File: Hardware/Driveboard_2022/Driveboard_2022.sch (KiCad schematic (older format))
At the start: 107 parts, among them SW1 SW_Push, SW2 SW_Push, SW3 SW_Push, SW4 SW_SPST, SW5 SW_Push, SW6 SW_Push, SW7 SW_Push, U1 TM4C129E_Launchpad, U2 MAX_3232, U3 MAX_3232, U4 MAX_3232, U5 OKI 3V3, U6 OKI 5V

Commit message: Removed Encoder, Fixed Resistor Values
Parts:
- removed Conn1, Conn2, Conn3, Conn4, Conn5, Conn6: Molex_uF_S_03, MRDT_Connectors:MOLEX_uF_S_03_Horizontal, symbol MRDT_Connectors:Molex_uF_S_03
- removed LED29, LED30, LED31, LED32, LED33, LED34: Blue, symbol Device:LED
- removed R29, R30, R31, R32, R33, R34: 330, symbol Device:R
- Conn13: symbol MRDT_Connectors:AndersonPP -> Driveboard_2022-rescue:AndersonPP-MRDT_Connectors
- R10: value 1k -> 330
- R11, R12, R13, R14, R15, R16, R8: value 330 -> 43
- R17, R18, R19, R20, R21, R22, R23, R24, R25, R26, R27, R28, R9: value 500 -> 100
- U2, U3, U4: symbol MRDT_ICs:MAX_3232 -> Driveboard_2022-rescue:MAX_3232-MRDT_ICs
- U5, U6: symbol MRDT_Devices:OKI -> Driveboard_2022-rescue:OKI-MRDT_Devices
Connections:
- net labels removed: BL_PWM, BR_PWM, FL_PWM, FR_PWM, ML_PWM, MR_PWM
- wire segments 373 -> 313
- no-connect marks 43 -> 49
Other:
- moved on the sheet: Conn10, Conn11, Conn12, Conn7, Conn8, Conn9

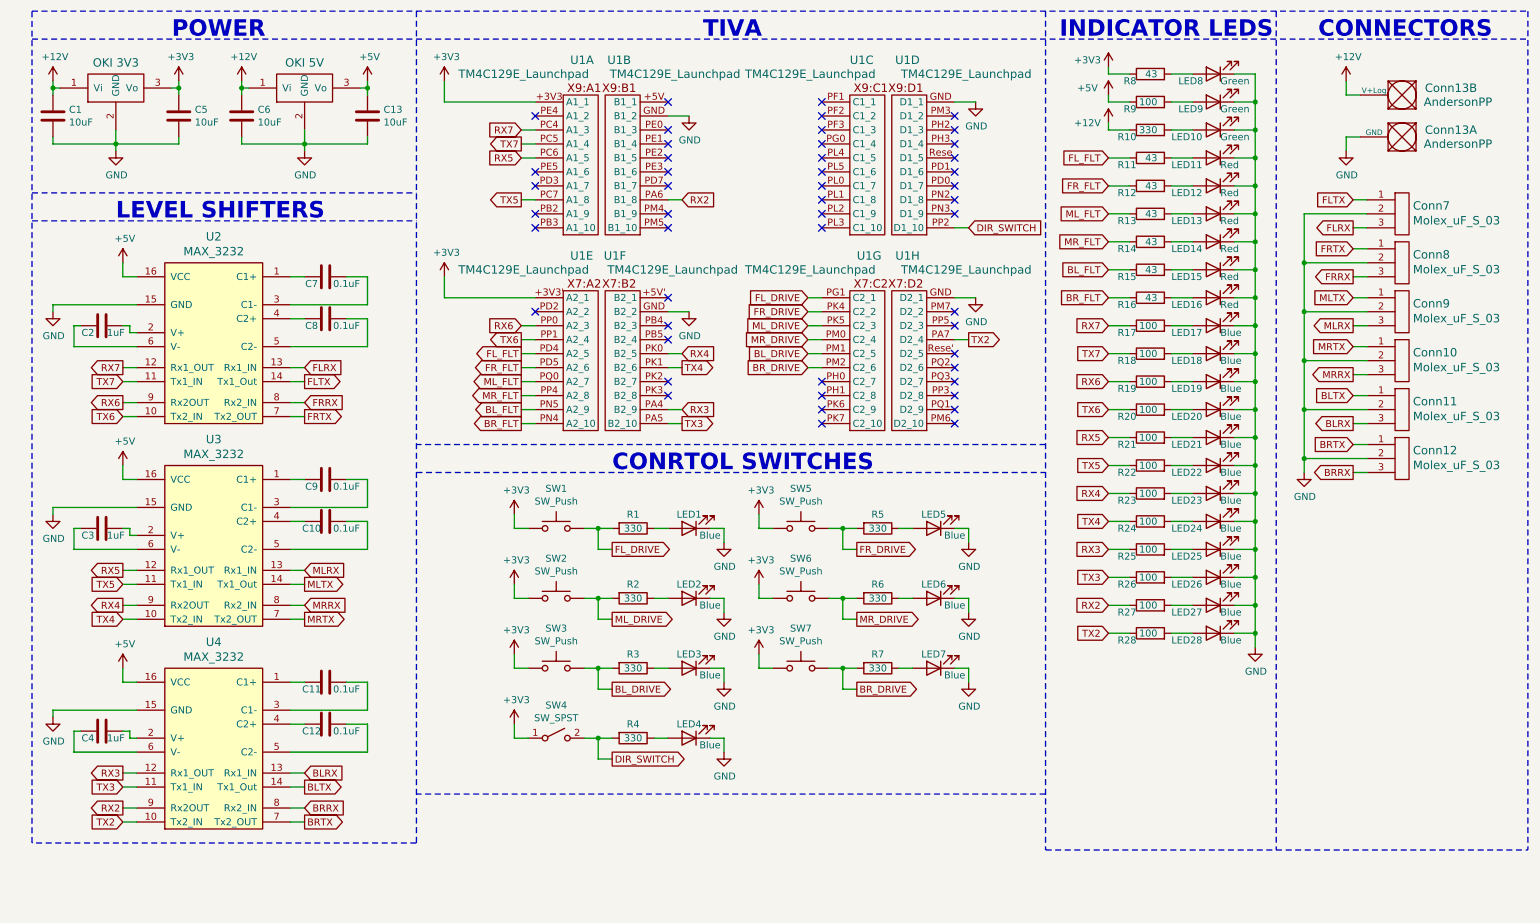
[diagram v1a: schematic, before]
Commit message: Added VESC Connectors, Fixed Switch Resistors
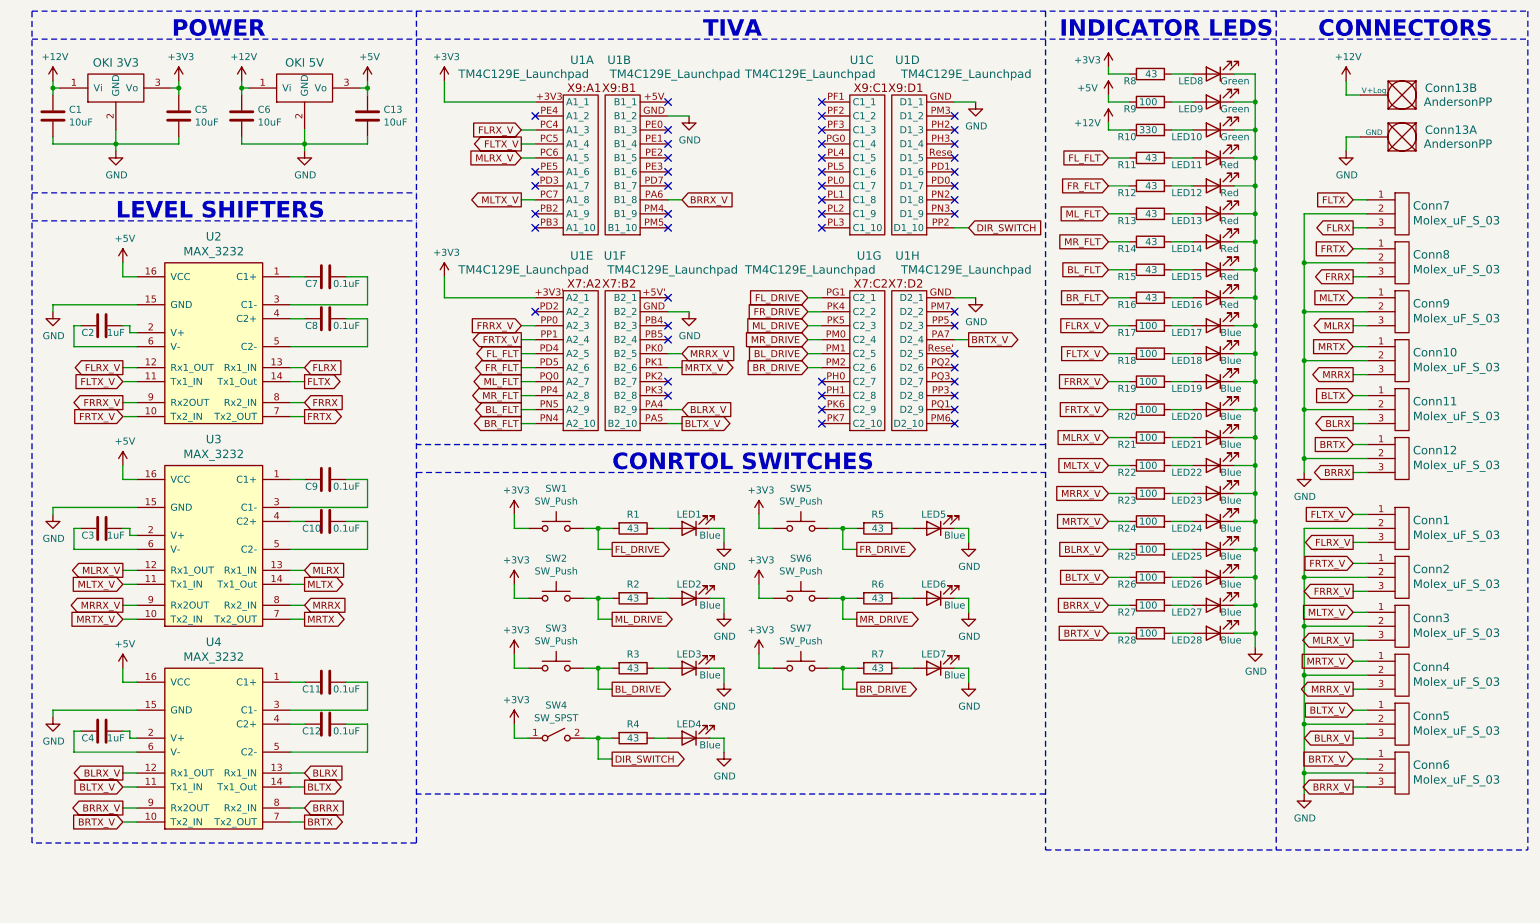
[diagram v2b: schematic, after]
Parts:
- added Conn1, Conn2, Conn3, Conn4, Conn5, Conn6: Molex_uF_S_03, MRDT_Connectors:MOLEX_uF_S_03_Horizontal, symbol MRDT_Connectors:Molex_uF_S_03
- R1, R2, R3, R4, R5, R6, R7: value 330 -> 43
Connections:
- net GND: now also Conn1.2, Conn2.2, Conn3.2, Conn4.2, Conn5.2, Conn6.2
- net RX2 renamed BRRX_V
- net BRRX_V: now also Conn6.3
- net RX3 renamed BLRX_V
- net BLRX_V: now also Conn5.3
- net RX4 renamed MRRX_V
- net MRRX_V: now also Conn4.3
- net RX5 renamed MLRX_V
- net MLRX_V: now also Conn3.3
- net RX6 renamed FRRX_V
- net FRRX_V: now also Conn2.3
- net RX7 renamed FLRX_V
- net FLRX_V: now also Conn1.3
- net TX2 renamed BRTX_V
- net BRTX_V: now also Conn6.1
- net TX3 renamed BLTX_V
- net BLTX_V: now also Conn5.1
- net TX4 renamed MRTX_V
- net MRTX_V: now also Conn4.1
- net TX5 renamed MLTX_V
- net MLTX_V: now also Conn3.1
- net TX6 renamed FRTX_V
- net FRTX_V: now also Conn2.1
- net TX7 renamed FLTX_V
- net FLTX_V: now also Conn1.1
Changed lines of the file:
@@
 	9600 3700 9600 3350
 Text GLabel 4000 1350 0    50   Input ~ 0
-RX7
+FLRX_V
 Wire Wire Line
 	4000 1350 4100 1350
 Text GLabel 4000 1450 0    50   Output ~ 0
-TX7
+FLTX_V
 Wire Wire Line
 	4000 1450 4100 1450
 Text GLabel 4000 1550 0    50   Input ~ 0
-RX5
+MLRX_V
 Wire Wire Line
 	4000 1550 4100 1550
 Text GLabel 4000 1850 0    50   Output ~ 0
-TX5
+MLTX_V
 Wire Wire Line
 	4000 1850 4100 1850
 Text GLabel 5150 1850 2    50   Input ~ 0
-RX2
+BRRX_V
 Wire Wire Line
 	5150 1850 5050 1850
 Text GLabel 7200 2850 2    50   Output ~ 0
-TX2
+BRTX_V
 Wire Wire Line
 	7200 2850 7100 2850
@@
 P 4800 4200
 F 0 "R1" V 4700 4200 50  0000 C CNN
-F 1 "330" V 4800 4200 50  0000 C CNN
+F 1 "43" V 4800 4200 50  0000 C CNN
 F 2 "" V 4730 4200 50  0001 C CNN
 F 3 "~" H 4800 4200 50  0001 C CNN
@@
 P 4800 4700
 F 0 "R2" V 4700 4700 50  0000 C CNN
-F 1 "330" V 4800 4700 50  0000 C CNN
+F 1 "43" V 4800 4700 50  0000 C CNN
 F 2 "" V 4730 4700 50  0001 C CNN
 F 3 "~" H 4800 4700 50  0001 C CNN
@@
 P 4800 5200
 F 0 "R3" V 4700 5200 50  0000 C CNN
-F 1 "330" V 4800 5200 50  0000 C CNN
+F 1 "43" V 4800 5200 50  0000 C CNN
 F 2 "" V 4730 5200 50  0001 C CNN
 F 3 "~" H 4800 5200 50  0001 C CNN
@@
 P 6550 4200
 F 0 "R5" V 6450 4200 50  0000 C CNN
-F 1 "330" V 6550 4200 50  0000 C CNN
+F 1 "43" V 6550 4200 50  0000 C CNN
 F 2 "" V 6480 4200 50  0001 C CNN
 F 3 "~" H 6550 4200 50  0001 C CNN
@@
 P 6550 4700
 F 0 "R6" V 6450 4700 50  0000 C CNN
-F 1 "330" V 6550 4700 50  0000 C CNN
+F 1 "43" V 6550 4700 50  0000 C CNN
 F 2 "" V 6480 4700 50  0001 C CNN
 F 3 "~" H 6550 4700 50  0001 C CNN
@@
 P 6550 5200
 F 0 "R7" V 6450 5200 50  0000 C CNN
-F 1 "330" V 6550 5200 50  0000 C CNN
+F 1 "43" V 6550 5200 50  0000 C CNN
 F 2 "" V 6480 5200 50  0001 C CNN
 F 3 "~" H 6550 5200 50  0001 C CNN
@@
 P 4800 5700
 F 0 "R4" V 4700 5700 50  0000 C CNN
-F 1 "330" V 4800 5700 50  0000 C CNN
+F 1 "43" V 4800 5700 50  0000 C CNN
 F 2 "" V 4730 5700 50  0001 C CNN
 F 3 "~" H 4800 5700 50  0001 C CNN
@@
 $EndComp
 Text GLabel 8200 4150 0    50   Input ~ 0
-TX4
+MRTX_V
 Wire Wire Line
 	9100 4150 9250 4150
@@
 $EndComp
 Text GLabel 8200 2950 0    50   Input ~ 0
-TX7
+FLTX_V
 $Comp
 L Device:R R20
@@
 	9100 4550 9250 4550
 Text GLabel 8200 3350 0    50   Input ~ 0
-TX6
+FRTX_V
 Text GLabel 8200 4550 0    50   Input ~ 0
-TX3
+BLTX_V
 $Comp
 L Device:R R19
@@
 	9100 4350 9250 4350
 Text GLabel 8200 3150 0    50   Input ~ 0
-RX6
+FRRX_V
 Text GLabel 8200 4350 0    50   Input ~ 0
-RX3
+BLRX_V
 $Comp
 L Device:R R17
@@
 	9100 3950 9250 3950
 Text GLabel 8200 2750 0    50   Input ~ 0
-RX7
+FLRX_V
 Text GLabel 8200 3950 0    50   Input ~ 0
-RX4
+MRRX_V
 $Comp
 L Device:LED LED20
@@
 $EndComp
 Text GLabel 8200 4750 0    50   Input ~ 0
-RX2
+BRRX_V
 Text GLabel 8200 3550 0    50   Input ~ 0
-RX5
+MLRX_V
 Wire Wire Line
 	9100 4750 9250 4750
@@
 $EndComp
 Text GLabel 8200 4950 0    50   Input ~ 0
-TX2
+BRTX_V
 Text GLabel 8200 3750 0    50   Input ~ 0
-TX5
+MLTX_V
 Wire Wire Line
 	9100 4950 9250 4950
@@
 FRTX
 Text GLabel 1150 3050 0    50   Output ~ 0
-RX7
+FLRX_V
 Text GLabel 1150 3150 0    50   Input ~ 0
-TX7
+FLTX_V
 Text GLabel 1150 3300 0    50   Output ~ 0
-RX6
+FRRX_V
 Text GLabel 1150 3400 0    50   Input ~ 0
-TX6
+FRTX_V
 Wire Wire Line
 	2450 3150 2350 3150
@@
 MRTX
 Text GLabel 1150 4500 0    50   Output ~ 0
-RX5
+MLRX_V
 Text GLabel 1150 4600 0    50   Input ~ 0
-TX5
+MLTX_V
 Text GLabel 1150 4750 0    50   Output ~ 0
-RX4
+MRRX_V
 Text GLabel 1150 4850 0    50   Input ~ 0
-TX4
+MRTX_V
 Wire Wire Line
 	2450 4600 2350 4600
@@
 BLTX
 Text GLabel 1150 5950 0    50   Output ~ 0
-RX3
+BLRX_V
 Text GLabel 1150 6050 0    50   Input ~ 0
-TX3
+BLTX_V
 Text GLabel 1150 6200 0    50   Output ~ 0
-RX2
+BRRX_V
 Text GLabel 1150 6300 0    50   Input ~ 0
-TX2
+BRTX_V
 Wire Wire Line
 	2450 6050 2350 6050
@@
 	5150 3350 5050 3350
 Text GLabel 5150 3450 2    50   Output ~ 0
-TX3
+BLTX_V
 Text GLabel 5150 3350 2    50   Input ~ 0
-RX3
+BLRX_V
 Wire Wire Line
 	5150 3050 5050 3050
 Text GLabel 5150 3050 2    50   Output ~ 0
-TX4
+MRTX_V
 Wire Wire Line
 	5150 2950 5050 2950
 Text GLabel 5150 2950 2    50   Input ~ 0
-RX4
+MRRX_V
 Wire Wire Line
 	4000 2850 4100 2850
 Text GLabel 4000 2850 0    50   Output ~ 0
-TX6
+FRTX_V
 Wire Wire Line
 	4000 2750 4100 2750
 Text GLabel 4000 2750 0    50   Input ~ 0
-RX6
+FRRX_V
 NoConn ~ 5050 2550
 Wire Wire Line
@@
 NoConn ~ 6150 1250
 NoConn ~ 6150 1150
+Text GLabel 9950 4100 0    50   Input ~ 0
+FLTX_V
+Text GLabel 9950 4300 0    50   Output ~ 0
+FLRX_V
+Text GLabel 9950 4450 0    50   Input ~ 0
+FRTX_V
+Text GLabel 9950 4650 0    50   Output ~ 0
+FRRX_V
+Text GLabel 9950 4800 0    50   Input ~ 0
+MLTX_V
+Text GLabel 9950 5000 0    50   Output ~ 0
+MLRX_V
+Text GLabel 9950 5150 0    50   Input ~ 0
+MRTX_V
+Text GLabel 9950 5350 0    50   Output ~ 0
+MRRX_V
+Text GLabel 9950 5500 0    50   Input ~ 0
+BLTX_V
+Text GLabel 9950 5700 0    50   Output ~ 0
+BLRX_V
+Wire Wire Line
+	9950 4100 10050 4100
+Wire Wire Line
+	9950 4300 10050 4300
+Wire Wire Line
+	9950 4450 10050 4450
+Wire Wire Line
+	9950 4650 10050 4650
+Wire Wire Line
+	9950 4800 10050 4800
+Wire Wire Line
+	9950 5000 10050 5000
+Wire Wire Line
+	9950 5150 10050 5150
+Wire Wire Line
+	9950 5350 10050 5350
+Wire Wire Line
+	9950 5500 10050 5500
+Wire Wire Line
+	9950 5700 10050 5700
+Wire Wire Line
+	9950 5850 10050 5850
+$Comp
+L power:GND #PWR036
+U 1 1 616895FA
+P 9600 6100
+F 0 "#PWR036" H 9600 5850 50  0001 C CNN
+F 1 "GND" H 9605 5927 50  0000 C CNN
+F 2 "" H 9600 6100 50  0001 C CNN
+F 3 "" H 9600 6100 50  0001 C CNN
+	1    9600 6100
+	1    0    0    -1
+$EndComp
+Wire Wire Line
+	9600 4200 10050 4200
+Wire Wire Line
+	10050 4550 9600 4550
+Connection ~ 9600 4550
+Wire Wire Line
+	9600 4550 9600 4200
+Wire Wire Line
+	10050 4900 9600 4900
+Connection ~ 9600 4900
+Wire Wire Line
+	9600 4900 9600 4550
+Wire Wire Line
+	10050 5250 9600 5250
+Connection ~ 9600 5250
+Wire Wire Line
+	9600 5250 9600 4900
+Wire Wire Line
+	10050 5600 9600 5600
+Connection ~ 9600 5600
+Wire Wire Line
+	9600 5600 9600 5250
+Wire Wire Line
+	10050 5950 9600 5950
+Wire Wire Line
+	9600 5950 9600 5600
+$Comp
+L MRDT_Connectors:Molex_uF_S_03 Conn1
+U 1 1 6168960F
+P 10250 4350
+F 0 "Conn1" H 10378 4558 60  0000 L CNN
+F 1 "Molex_uF_S_03" H 10378 4452 60  0000 L CNN
+F 2 "MRDT_Connectors:MOLEX_uF_S_03_Horizontal" H 10250 4350 60  0001 C CNN
+F 3 "" H 10250 4350 60  0001 C CNN
+	1    10250 4350
+	1    0    0    -1
+$EndComp
+$Comp
+L MRDT_Connectors:Molex_uF_S_03 Conn2
+U 1 1 61689615
+P 10250 4700
+F 0 "Conn2" H 10378 4908 60  0000 L CNN
+F 1 "Molex_uF_S_03" H 10378 4802 60  0000 L CNN
+F 2 "MRDT_Connectors:MOLEX_uF_S_03_Horizontal" H 10250 4700 60  0001 C CNN
+F 3 "" H 10250 4700 60  0001 C CNN
+	1    10250 4700
+	1    0    0    -1
+$EndComp
+$Comp
+L MRDT_Connectors:Molex_uF_S_03 Conn3
+U 1 1 6168961B
+P 10250 5050
+F 0 "Conn3" H 10378 5258 60  0000 L CNN
+F 1 "Molex_uF_S_03" H 10378 5152 60  0000 L CNN
+F 2 "MRDT_Connectors:MOLEX_uF_S_03_Horizontal" H 10250 5050 60  0001 C CNN
+F 3 "" H 10250 5050 60  0001 C CNN
+	1    10250 5050
+	1    0    0    -1
+$EndComp
+$Comp
+L MRDT_Connectors:Molex_uF_S_03 Conn4
+U 1 1 61689621
+P 10250 5400
+F 0 "Conn4" H 10378 5608 60  0000 L CNN
+F 1 "Molex_uF_S_03" H 10378 5502 60  0000 L CNN
+F 2 "MRDT_Connectors:MOLEX_uF_S_03_Horizontal" H 10250 5400 60  0001 C CNN
+F 3 "" H 10250 5400 60  0001 C CNN
+	1    10250 5400
+	1    0    0    -1
+$EndComp
+$Comp
+L MRDT_Connectors:Molex_uF_S_03 Conn5
+U 1 1 61689627
+P 10250 5750
+F 0 "Conn5" H 10378 5958 60  0000 L CNN
+F 1 "Molex_uF_S_03" H 10378 5852 60  0000 L CNN
+F 2 "MRDT_Connectors:MOLEX_uF_S_03_Horizontal" H 10250 5750 60  0001 C CNN
+F 3 "" H 10250 5750 60  0001 C CNN
+	1    10250 5750
+	1    0    0    -1
+$EndComp
+$Comp
+L MRDT_Connectors:Molex_uF_S_03 Conn6
+U 1 1 6168962D
+P 10250 6100
+F 0 "Conn6" H 10378 6308 60  0000 L CNN
+F 1 "Molex_uF_S_03" H 10378 6202 60  0000 L CNN
+F 2 "MRDT_Connectors:MOLEX_uF_S_03_Horizontal" H 10250 6100 60  0001 C CNN
+F 3 "" H 10250 6100 60  0001 C CNN
+	1    10250 6100
+	1    0    0    -1
+$EndComp
+Connection ~ 9600 5950
+Text GLabel 9950 5850 0    50   Input ~ 0
+BRTX_V
+Text GLabel 9950 6050 0    50   Output ~ 0
+BRRX_V
+Wire Wire Line
+	10050 6050 9950 6050
+Wire Wire Line
+	9600 5950 9600 6100
 $EndSCHEMATC

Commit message: Slide Switches
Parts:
- removed SW1, SW2, SW3, SW5, SW6, SW7: SW_Push, symbol Switch:SW_Push
- added SW1, SW2, SW3, SW5, SW6, SW7: SW_SPST, symbol Switch:SW_SPST
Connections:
- net +3V3: now also SW1.1 (A), SW2.1 (A), SW3.1 (A), SW5.1 (A), SW6.1 (A), SW7.1 (A)
- net BL_DRIVE: now also SW3.2 (B)
- net BR_DRIVE: now also SW7.2 (B)
- net FL_DRIVE: now also SW1.2 (B)
- net FR_DRIVE: now also SW5.2 (B)
- net ML_DRIVE: now also SW2.2 (B)
- net MR_DRIVE: now also SW6.2 (B)
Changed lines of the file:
@@
-$EndComp
-$Comp
-L Switch:SW_Push SW1
-U 1 1 615BDC81
-P 4250 4200
-F 0 "SW1" H 4250 4485 50  0000 C CNN
-F 1 "SW_Push" H 4250 4394 50  0000 C CNN
-F 2 "" H 4250 4400 50  0001 C CNN
-F 3 "~" H 4250 4400 50  0001 C CNN
-	1    4250 4200
-	1    0    0    -1
 $EndComp
 $Comp
@@
 $EndComp
 $Comp
-L Switch:SW_Push SW2
-U 1 1 615E5C83
-P 4250 4700
-F 0 "SW2" H 4250 4985 50  0000 C CNN
-F 1 "SW_Push" H 4250 4894 50  0000 C CNN
-F 2 "" H 4250 4900 50  0001 C CNN
-F 3 "~" H 4250 4900 50  0001 C CNN
-	1    4250 4700
-	1    0    0    -1
-$EndComp
-$Comp
 L Device:R R2
 U 1 1 615E5C89
@@
 $EndComp
 $Comp
-L Switch:SW_Push SW3
-U 1 1 615ED99C
-P 4250 5200
-F 0 "SW3" H 4250 5485 50  0000 C CNN
-F 1 "SW_Push" H 4250 5394 50  0000 C CNN
-F 2 "" H 4250 5400 50  0001 C CNN
-F 3 "~" H 4250 5400 50  0001 C CNN
-	1    4250 5200
-	1    0    0    -1
-$EndComp
-$Comp
 L Device:R R3
 U 1 1 615ED9A2
@@
 $EndComp
 $Comp
-L Switch:SW_Push SW5
-U 1 1 6160311C
-P 6000 4200
-F 0 "SW5" H 6000 4485 50  0000 C CNN
-F 1 "SW_Push" H 6000 4394 50  0000 C CNN
-F 2 "" H 6000 4400 50  0001 C CNN
-F 3 "~" H 6000 4400 50  0001 C CNN
-	1    6000 4200
-	1    0    0    -1
-$EndComp
-$Comp
 L Device:R R5
 U 1 1 61603122
@@
 $EndComp
 $Comp
-L Switch:SW_Push SW6
-U 1 1 61603145
-P 6000 4700
-F 0 "SW6" H 6000 4985 50  0000 C CNN
-F 1 "SW_Push" H 6000 4894 50  0000 C CNN
-F 2 "" H 6000 4900 50  0001 C CNN
-F 3 "~" H 6000 4900 50  0001 C CNN
-	1    6000 4700
-	1    0    0    -1
-$EndComp
-$Comp
 L Device:R R6
 U 1 1 6160314B
@@
 F 3 "" H 5700 5100 50  0001 C CNN
 	1    5700 5100
-	1    0    0    -1
-$EndComp
-$Comp
-L Switch:SW_Push SW7
-U 1 1 6160316E
-P 6000 5200
-F 0 "SW7" H 6000 5485 50  0000 C CNN
-F 1 "SW_Push" H 6000 5394 50  0000 C CNN
-F 2 "" H 6000 5400 50  0001 C CNN
-F 3 "~" H 6000 5400 50  0001 C CNN
-	1    6000 5200
 	1    0    0    -1
 $EndComp
@@
 Wire Wire Line
 	9600 5950 9600 6100
+$Comp
+L Switch:SW_SPST SW3
+U 1 1 616C949B
+P 4250 5200
+F 0 "SW3" H 4250 5435 50  0000 C CNN
+F 1 "SW_SPST" H 4250 5344 50  0000 C CNN
+F 2 "" H 4250 5200 50  0001 C CNN
+F 3 "~" H 4250 5200 50  0001 C CNN
+	1    4250 5200
+	1    0    0    -1
+$EndComp
+$Comp
+L Switch:SW_SPST SW2
+U 1 1 616EF582
+P 4250 4700
+F 0 "SW2" H 4250 4935 50  0000 C CNN
+F 1 "SW_SPST" H 4250 4844 50  0000 C CNN
+F 2 "" H 4250 4700 50  0001 C CNN
+F 3 "~" H 4250 4700 50  0001 C CNN
+	1    4250 4700
+	1    0    0    -1
+$EndComp
+$Comp
+L Switch:SW_SPST SW1
+U 1 1 61715659
+P 4250 4200
+F 0 "SW1" H 4250 4435 50  0000 C CNN
+F 1 "SW_SPST" H 4250 4344 50  0000 C CNN
+F 2 "" H 4250 4200 50  0001 C CNN
+F 3 "~" H 4250 4200 50  0001 C CNN
+	1    4250 4200
+	1    0    0    -1
+$EndComp
+$Comp
+L Switch:SW_SPST SW5
+U 1 1 6173B76C
+P 6000 4200
+F 0 "SW5" H 6000 4435 50  0000 C CNN
+F 1 "SW_SPST" H 6000 4344 50  0000 C CNN
+F 2 "" H 6000 4200 50  0001 C CNN
+F 3 "~" H 6000 4200 50  0001 C CNN
+	1    6000 4200
+	1    0    0    -1
+$EndComp
+$Comp
+L Switch:SW_SPST SW6
+U 1 1 617618B1
+P 6000 4700
+F 0 "SW6" H 6000 4935 50  0000 C CNN
+F 1 "SW_SPST" H 6000 4844 50  0000 C CNN
+F 2 "" H 6000 4700 50  0001 C CNN
+F 3 "~" H 6000 4700 50  0001 C CNN
+	1    6000 4700
+	1    0    0    -1
+$EndComp
+$Comp
+L Switch:SW_SPST SW7
+U 1 1 617878FC
+P 6000 5200
+F 0 "SW7" H 6000 5435 50  0000 C CNN
+F 1 "SW_SPST" H 6000 5344 50  0000 C CNN
+F 2 "" H 6000 5200 50  0001 C CNN
+F 3 "~" H 6000 5200 50  0001 C CNN
+	1    6000 5200
+	1    0    0    -1
+$EndComp
 $EndSCHEMATC
